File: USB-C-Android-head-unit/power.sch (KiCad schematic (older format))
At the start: 0 parts

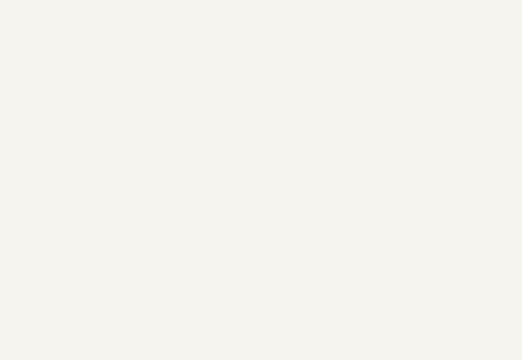
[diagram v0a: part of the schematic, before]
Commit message: work on USB hub
Also changed sheet sizes
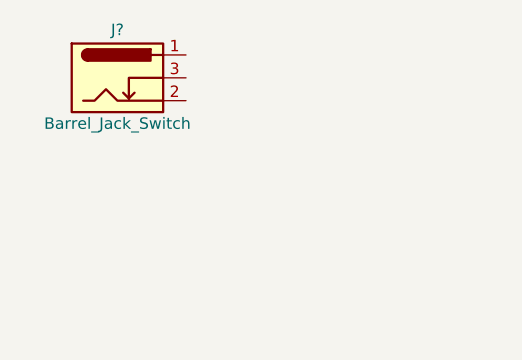
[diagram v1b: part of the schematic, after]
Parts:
- added J?: Barrel_Jack_Switch, symbol Connector:Barrel_Jack_Switch
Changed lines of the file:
@@
 EELAYER 30 0
 EELAYER END
-$Descr A4 11693 8268
+$Descr USLetter 11000 8500
 encoding utf-8
 Sheet 4 7
-Title ""
+Title "Power Distribution"
 Date ""
 Rev ""
@@
 Text Notes 4550 3450 0    50   ~ 0
 VBUS is power input from one and only one USB C jack at a time.
+$Comp
+L Connector:Barrel_Jack_Switch J?
+U 1 1 5E206029
+P 2000 2250
+F 0 "J?" H 2000 2460 50  0000 C CNN
+F 1 "Barrel_Jack_Switch" H 2000 2050 50  0000 C CNN
+F 2 "" H 2050 2210 50  0001 C CNN
+F 3 "~" H 2050 2210 50  0001 C CNN
+	1    2000 2250
+	1    0    0    -1
+$EndComp
 $EndSCHEMATC

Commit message: not sure what changed here
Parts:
- removed J?: Barrel_Jack_Switch, symbol Connector:Barrel_Jack_Switch
- added J?: Barrel_Jack_Switch_Shield, SW-CUI-INC:PJ-047AH, symbol SW-con:Barrel_Jack_Switch_Shield
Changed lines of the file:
@@
 VBUS is power input from one and only one USB C jack at a time.
 $Comp
-L Connector:Barrel_Jack_Switch J?
-U 1 1 5E206029
-P 2000 2250
-F 0 "J?" H 2000 2460 50  0000 C CNN
-F 1 "Barrel_Jack_Switch" H 2000 2050 50  0000 C CNN
-F 2 "" H 2050 2210 50  0001 C CNN
-F 3 "~" H 2050 2210 50  0001 C CNN
-	1    2000 2250
+L SW-con:Barrel_Jack_Switch_Shield J?
+U 1 1 5D8B6C13
+P 1900 2250
+F 0 "J?" H 1900 2460 50  0000 C CNN
+F 1 "Barrel_Jack_Switch_Shield" H 1950 2000 50  0000 L CNN
+F 2 "SW-CUI-INC:PJ-047AH" H 1950 2210 50  0001 C CNN
+F 3 "https://www.cui.com/product/resource/pj-047ah.pdf" H 1950 2210 50  0001 C CNN
+F 4 "2.1x5.5mm" H 1900 2250 50  0001 C CNN "Characteristics"
+F 5 "CUI INC" H 1900 2250 50  0001 C CNN "Manufacturer"
+F 6 "Barrel Jack" H 1900 2250 50  0001 C CNN "Description"
+F 7 "Through hole" H 1900 2250 50  0001 C CNN "Package ID"
+F 8 "PJ-047AH" H 1900 2250 50  0001 C CNN "MPN"
+	1    1900 2250
 	1    0    0    -1
 $EndComp
